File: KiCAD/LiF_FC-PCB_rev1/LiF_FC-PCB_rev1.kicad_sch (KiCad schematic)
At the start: 0 parts

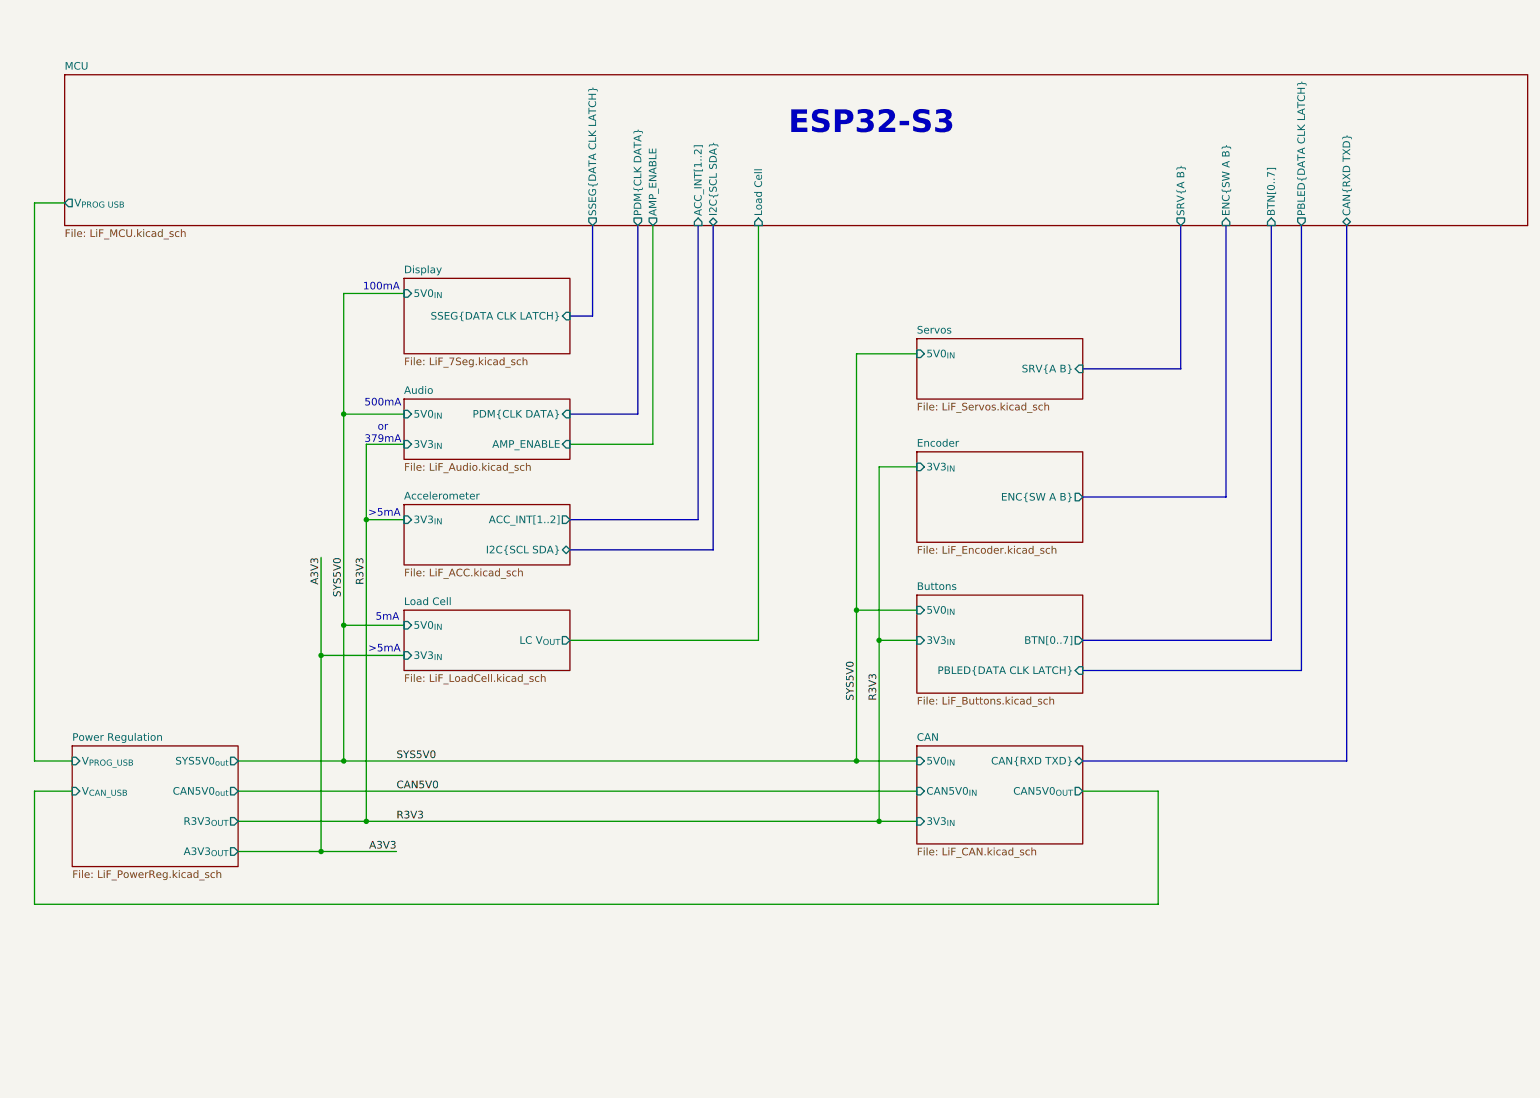
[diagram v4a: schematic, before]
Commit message: fixing ERC bugs on schematic. Only MCU left
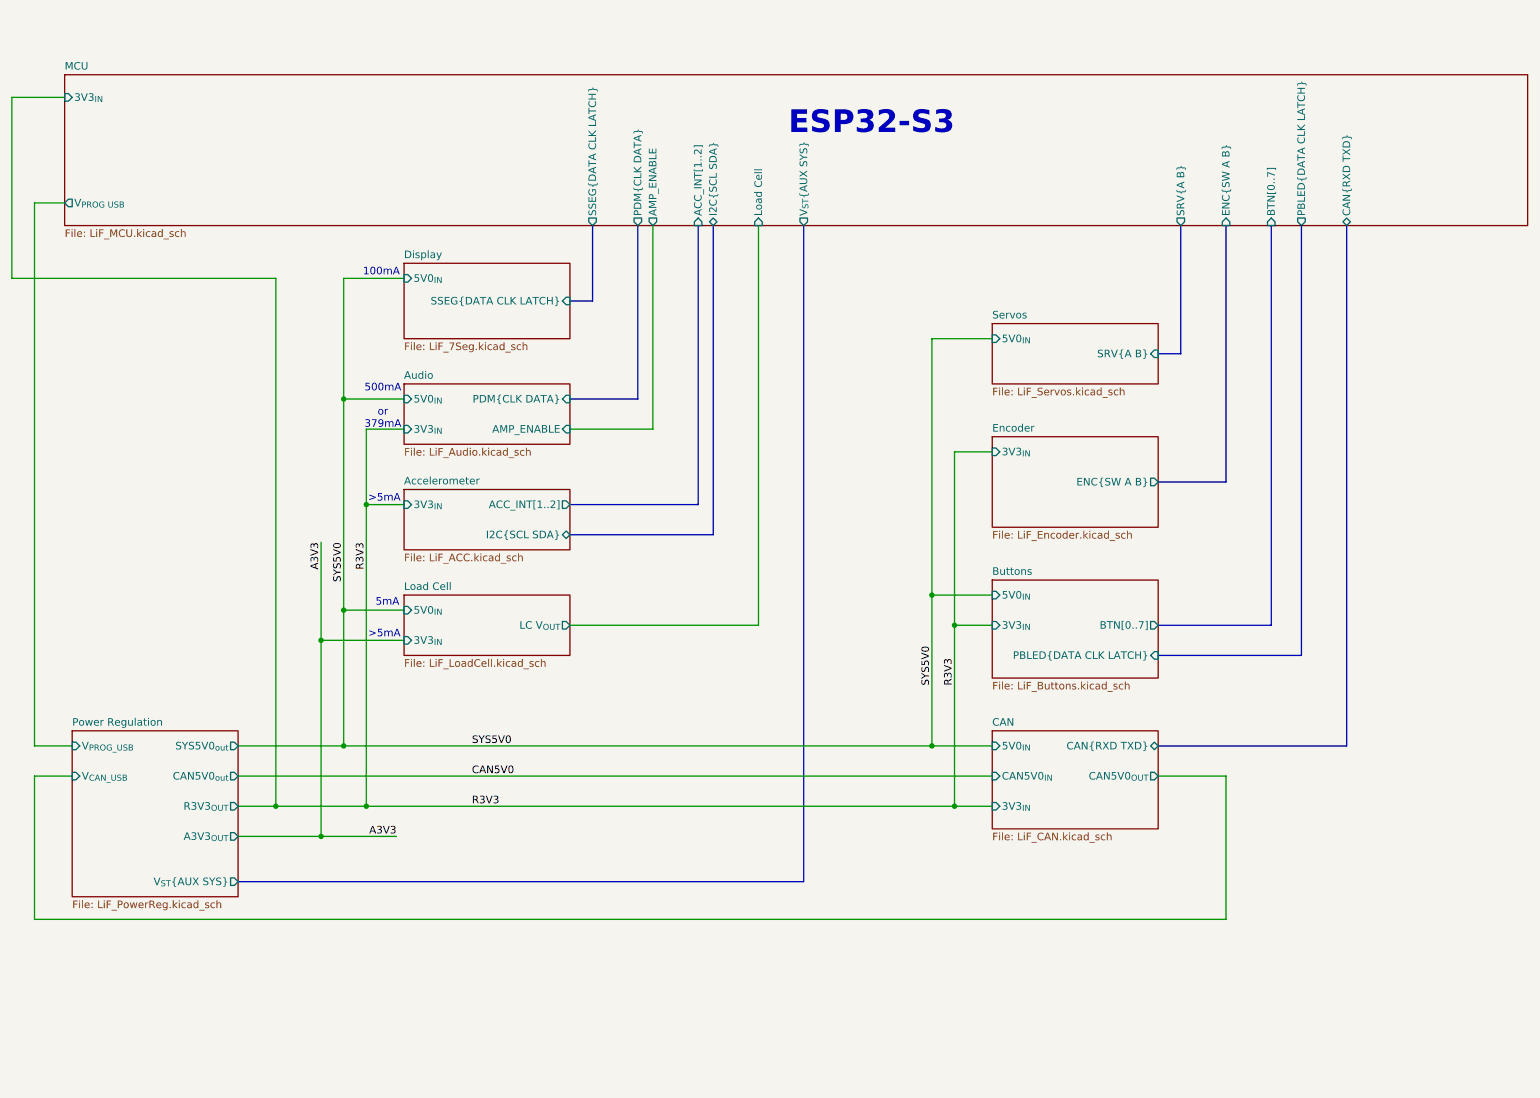
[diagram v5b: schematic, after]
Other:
- sheet MCU ports: added 3V3_{IN}, V_{ST}{AUX SYS}; removed none
- sheet Power Regulation ports: added V_{ST}{AUX SYS}; removed none

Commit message: Added MCU pinout, shanged shift registers to GPIO expanders to save pins on MCU
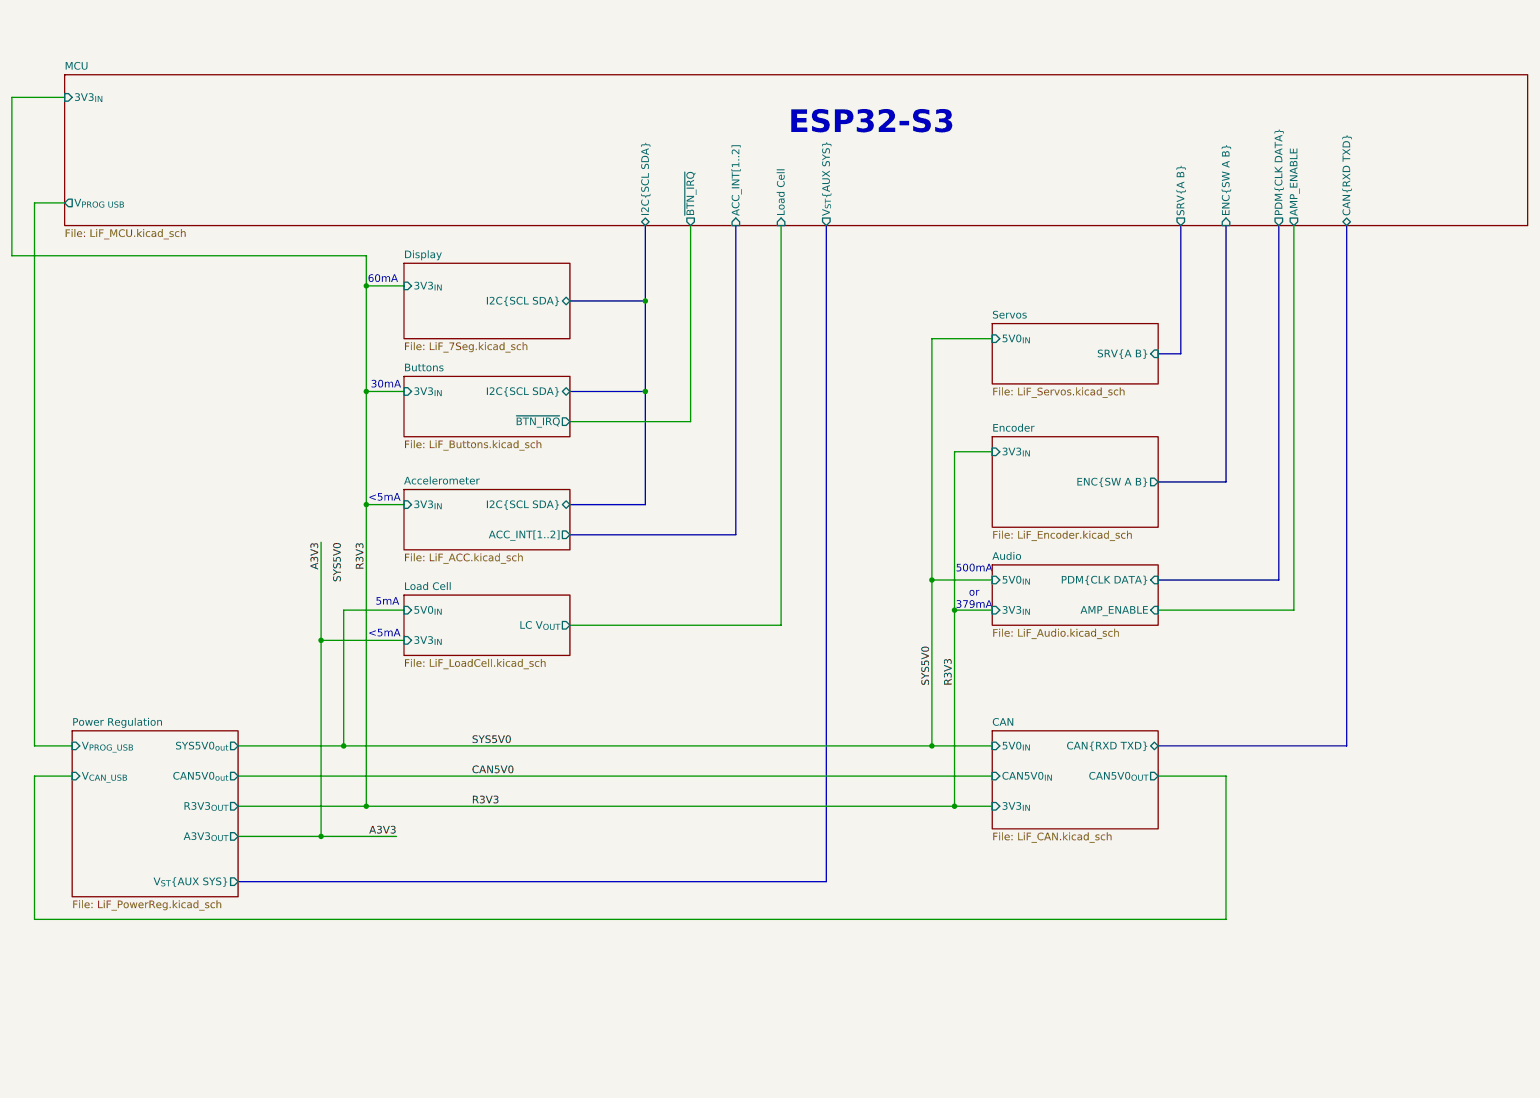
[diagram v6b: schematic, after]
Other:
- sheet Buttons ports: added I2C{SCL SDA}, ~{BTN_IRQ}; removed 5V0_{IN}, BTN[0..7], PBLED{DATA CLK LATCH}
- sheet Display ports: added 3V3_{IN}, I2C{SCL SDA}; removed 5V0_{IN}, SSEG{DATA CLK LATCH}
- sheet MCU ports: added ~{BTN_IRQ}; removed BTN[0..7], PBLED{DATA CLK LATCH}, SSEG{DATA CLK LATCH}
- note added: "30mA"
- note added: "60mA"
- note added: "<5mA"
- note removed: "100mA"
- note removed: ">5mA"
- title: (none) -> Lithium Firefly Custom FC/CC PCB

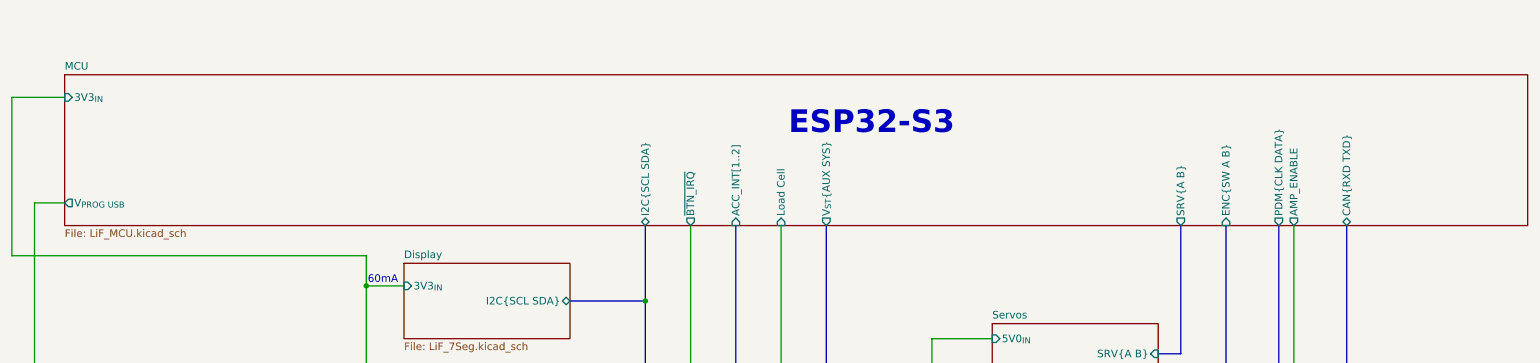
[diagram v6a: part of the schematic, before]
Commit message: Finalized schematic diagram. Only needs formatting fixes and resistor component sourcing info
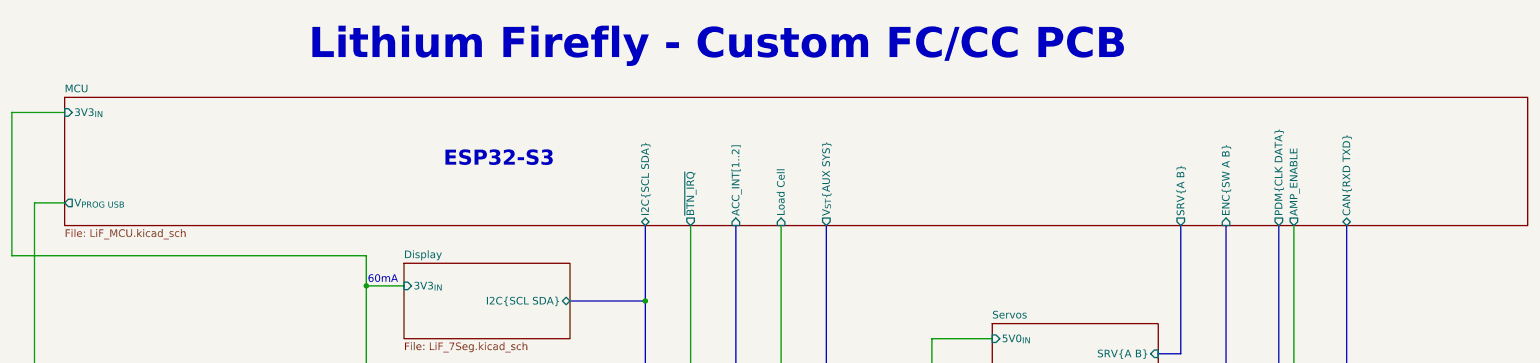
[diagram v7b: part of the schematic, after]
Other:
- note added: "Lithium Firefly - Custom FC/CC PCB"
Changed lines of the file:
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@@
+		)
+	)
+	(text "Lithium Firefly - Custom FC/CC PCB"
+		(exclude_from_sim no)
+		(at 134.112 17.78 0)
+		(effects
+			(font
+				(size 5.08 5.08)
+				(thickness 0.762)
+				(bold yes)
+			)
 		)
 	)
@@
 	(text "ESP32-S3"
 		(exclude_from_sim no)
-		(at 160.02 30.988 0)
+		(at 97.282 37.084 0)
 		(effects
 			(font
-				(size 3.81 3.81)
+				(size 2.54 2.54)
 				(thickness 0.762)
 				(bold yes)
@@
 	(wire
 		(pts
-			(xy 15.24 53.34) (xy 15.24 26.67)
+			(xy 15.24 53.34) (xy 15.24 29.21)
 		)
 		(stroke
@@
 	(wire
 		(pts
-			(xy 15.24 26.67) (xy 24.13 26.67)
+			(xy 15.24 29.21) (xy 24.13 29.21)
 		)
 		(stroke
@@
 	)
 	(sheet
-		(at 24.13 22.86)
-		(size 246.38 25.4)
+		(at 24.13 26.67)
+		(size 246.38 21.59)
 		(exclude_from_sim no)
 		(in_bom yes)
@@
 		)
 		(property "Sheetname" "MCU"
-			(at 24.13 22.1484 0)
+			(at 24.13 25.9584 0)
 			(effects
 				(font
@@
 		)
 		(pin "3V3_{IN}" input
-			(at 24.13 26.67 180)
-			(effects
-				(font
+			(at 24.13 29.21 180)
+			(effects
+				(font
